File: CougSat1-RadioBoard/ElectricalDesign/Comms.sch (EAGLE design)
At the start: 411 parts, among them J1 230mm Antenna, J2 CougSat Card, J3 700mm Antenna, J4 SWD, Q1 CSD25402Q3A, Q12 DMN53D0LDW, Q2 CSD25402Q3A, Q3 DMN53D0LDW, Q9 DMN53D0LDW, U1 INA199C1, U10 HMC452QS16G, U11 AD8515, U12 AD7291, U13 AD8515, U14 LP5907MFX-3.1, U15 AD9761, U16 TXS0102DQM, U18 TXS0102DQM, U19 MMZ09332B, U2 LP5907MFX-3.1, U20 ADF4360, U21 HMC545A, U22 AD9761, U23 MAAM-011229, U24 AD8515, U25 MAAM-011229, U26 AD8345, U28 AD8348, U29 AD7291, U3 TPS61236, U30 TXS0102DQM, U31 MAAM-011229, U32 AD8515, U35 TXS0102DQM, U36 ADF4360, U37 MAAM-011229, U39 AD8515, U4 AD8346, U40 AD8515, U42 TXS0102DQM, U43 INA199C2, U44 TXS0102DQM, U45 TXS0102DQM, U46 TXS0102DQM, U47 TXS0102DQM, U48 AD7291, U49 AD8515, U5 ADF4360, U50 INA199C2, U51 LP5907MFX-3.1, U52 INA199C2, U53 INA199C1, U54 TXS0102DQM, U55 TXS0102DQM, U6 STM32L496VGT, U7 GRF2133, U8 IS25LP016D, U9 IS25LP016D, Y1 19.68MHz ±2.5ppm, Y2 8MHz ±10ppm, Y3 32.768kHz ±10ppm, Y4 19.68MHz ±2.5ppm, Y5 19.68MHz ±2.5ppm

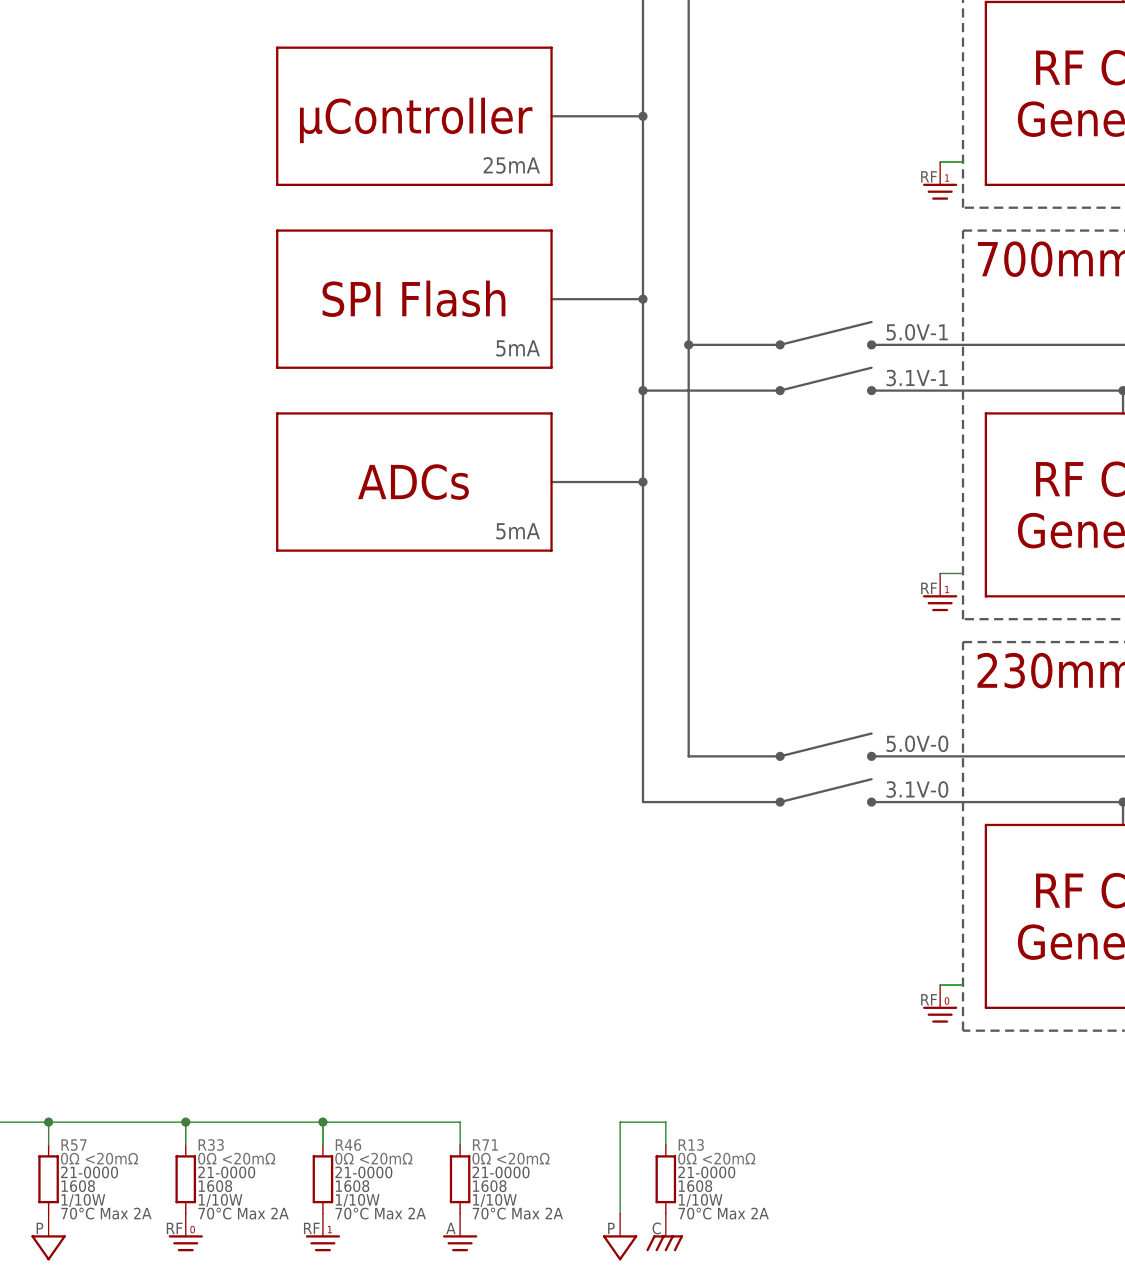
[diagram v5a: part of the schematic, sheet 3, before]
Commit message: Changed isolated ground to a solid DGND and relaying on layout to ensure good layout
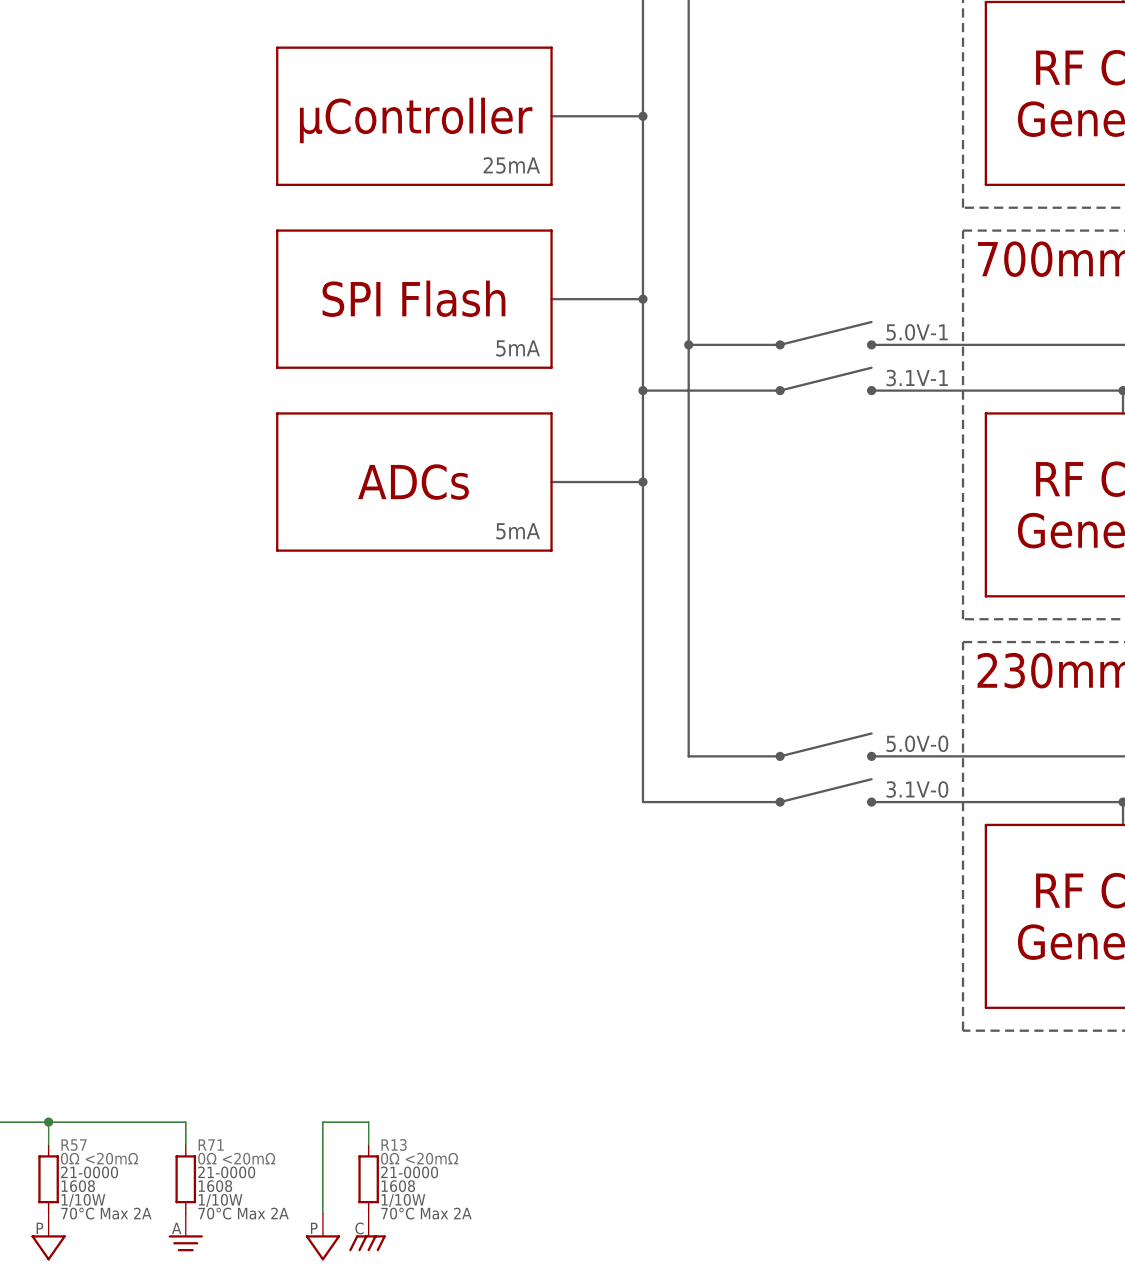
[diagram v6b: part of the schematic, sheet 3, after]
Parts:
- removed R33, R46: 0Ω <20mΩ, CougsInSpace-Resistors:RES-V-0-1608
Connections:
- removed net RFGND-0: C109.2, C114.2, C116.2, C132.2, C151.2, C16.2, C163.2, C18.2, C27.2, C33.2, C34.2, C39.2, C43.2, C51.2, C52.2, C53.2, C54.2, C79.2, C83.2, H4.SHIELD, J1.SHIELD, L13.1, L14.1, L18.1, L21.1, L4.1, R12.1, R19.1, R26.1, R33.1, R50.1, R51.1, R52.1, R55.1, U10.RFGND, U22.AVSS, U22.REFLO, U4.DGND, U4.RFGND, U5.AGND, U5.CPGND, U5.DGND, U5.PAD, U7.RFGND, Y1.GND
- new net N$7: L12.1, R83.1
- net DGND: now also C101.2, C105.2, C108.2, C109.2, C110.2, C111.2, C112.2, C113.2, C114.2, C116.2, C117.2, C118.2, C119.2, C120.2, C121.2, C122.2, C123.2, C124.1, C128.2, C129.2, C130.2, C132.2, C135.2, C136.2, C137.2, C139.2, C140.2, C143.2, C144.2, C145.2, C146.2, C147.2, C148.2, C151.2, C152.2, C153.2, C154.2, C155.2, C156.2, C16.2, C163.2, C18.2, C185.2, C188.2, C189.2, C191.2, C192.2, C194.2, C195.2, C196.2, C198.2, C199.2, C201.2, C204.2, C27.2, C29.2, C3.2, C33.2, C34.2, C35.2, C39.2, C43.2, C44.2, C46.2, C51.2, C52.2, C53.2, C54.2, C55.2, C56.2, C66.2, C67.2, C68.2, C71.2, C72.2, C73.2, C74.2, C79.2, C80.2, C83.2, C85.2, C88.2, C89.2, C90.2, C91.2, C94.2, C96.2, H4.SHIELD, H7.SHIELD, H8.SHIELD, J1.SHIELD, J3.SHIELD, L10.1, L11.1, L13.1, L14.1, L16.1, L18.1, L19.1, L21.1, L4.1, L9.1, Q12A.S, Q12B.S, Q3A.S, Q3B.D, Q3B.G, Q3B.S, Q9A.S, Q9B.S, R112.1, R12.1, R19.1, R2.1, R26.1, R32.1, R38.1, R40.1, R42.1, R45.1, R48.1, R50.1, R51.1, R52.1, R55.1, R61.1, R64.1, R68.1, R69.1, R70.1, R72.1, R77.1, R79.1, R84.1, R85.1, U10.RFGND, U15.AVSS, U15.REFLO, U20.AGND, U20.CPGND, U20.DGND, U20.PAD, U21.RFGND, U22.AVSS, U22.REFLO, U23.RFGND, U25.RFGND, U26.DGND, U26.RFGND, U28.DGND, U28.RFGND, U31.RFGND, U36.AGND, U36.CPGND, U36.DGND, U36.PAD, U37.RFGND, U4.DGND, U4.RFGND, U5.AGND, U5.CPGND, U5.DGND, U5.PAD, U7.RFGND, Y1.GND, Y4.GND, Y5.GND; no longer R33.2, R46.2
- net PGND: no longer C130.2, C3.2, C55.2, C56.2, Q9A.S, Q9B.S, R112.1, R2.1, R32.1, R40.1
- net RFGND-1: no longer C101.2, C105.2, C108.2, C110.2, C111.2, C112.2, C113.2, C117.2, C118.2, C119.2, C120.2, C121.2, C122.2, C123.2, C124.1, C128.2, C129.2, C135.2, C136.2, C137.2, C139.2, C140.2, C143.2, C144.2, C145.2, C146.2, C147.2, C148.2, C152.2, C153.2, C154.2, C155.2, C156.2, C185.2, C188.2, C189.2, C191.2, C192.2, C194.2, C195.2, C196.2, C198.2, C199.2, C201.2, C204.2, C29.2, C35.2, C44.2, C46.2, C66.2, C67.2, C68.2, C71.2, C72.2, C73.2, C74.2, C80.2, C85.2, C88.2, C89.2, C90.2, C91.2, C94.2, C96.2, H7.SHIELD, H8.SHIELD, J3.SHIELD, L10.1, L11.1, L12.1, L16.1, L19.1, L9.1, Q12A.S, Q12B.S, Q3A.S, Q3B.D, Q3B.G, Q3B.S, R38.1, R42.1, R45.1, R46.1, R48.1, R61.1, R64.1, R68.1, R69.1, R70.1, R72.1, R77.1, R79.1, R83.1, R84.1, R85.1, U15.AVSS, U15.REFLO, U20.AGND, U20.CPGND, U20.DGND, U20.PAD, U21.RFGND, U23.RFGND, U25.RFGND, U26.DGND, U26.RFGND, U28.DGND, U28.RFGND, U31.RFGND, U36.AGND, U36.CPGND, U36.DGND, U36.PAD, U37.RFGND, Y4.GND, Y5.GND
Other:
- moved on the sheet: R13, R71

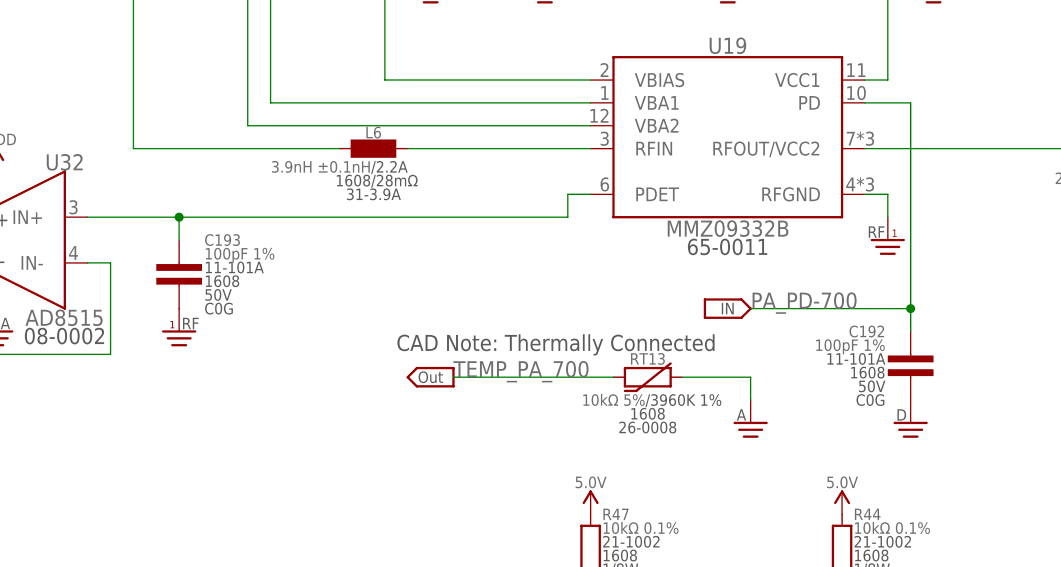
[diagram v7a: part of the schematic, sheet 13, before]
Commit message: Laid out 700mm modulator
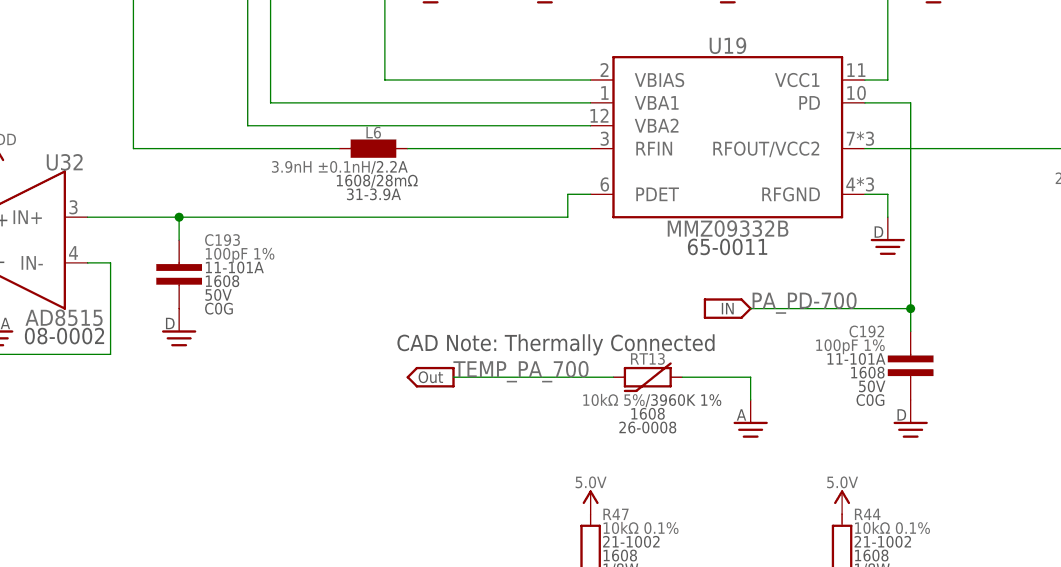
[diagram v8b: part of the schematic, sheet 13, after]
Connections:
- removed net N$7: L12.1, R83.1
- removed net RFGND-1: C193.2, U19.RFGND
- net DGND: now also C193.2, L12.1, R83.1, U19.RFGND
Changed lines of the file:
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@@
 <part name="L20" library="CougsInSpace-Coils" deviceset="INDUCTOR-H" device="-1608" technology="-56NH" value="56nH 2%"/>
 <part name="C67" library="CougsInSpace-Capacitors" deviceset="CAP-V" device="-1608" technology="-47PF" value="47pF 5%"/>
-<part name="SUPPLY246" library="CougsInSpace-PowerSymbols" deviceset="RFGND-1" device=""/>
-<part name="SUPPLY247" library="CougsInSpace-PowerSymbols" deviceset="RFGND-1" device=""/>
 <part name="C202" library="CougsInSpace-Capacitors" deviceset="CAP-H" device="-1608" technology="-220PF" value="220pF 1%"/>
 <part name="SUPPLY263" library="CougsInSpace-PowerSymbols" deviceset="5.0V-1" device=""/>
@@
 <part name="SUPPLY309" library="CougsInSpace-PowerSymbols" deviceset="DGND" device=""/>
 <part name="SUPPLY310" library="CougsInSpace-PowerSymbols" deviceset="DGND" device=""/>
+<part name="SUPPLY246" library="CougsInSpace-PowerSymbols" deviceset="DGND" device=""/>
+<part name="SUPPLY247" library="CougsInSpace-PowerSymbols" deviceset="DGND" device=""/>
+<part name="SUPPLY325" library="CougsInSpace-PowerSymbols" deviceset="DGND" device=""/>
 </parts>
 <sheets>
@@
 <instance part="SUPPLY191" gate="1" x="83.82" y="162.56" smashed="yes"/>
 <instance part="SUPPLY198" gate="1" x="20.32" y="170.18" smashed="yes"/>
+<instance part="SUPPLY325" gate="1" x="218.44" y="132.08" smashed="yes"/>
 </instances>
 <busses>
@@
 <pinref part="SUPPLY198" gate="1" pin="DGND"/>
 </segment>
+<segment>
+<pinref part="L12" gate="G$1" pin="1"/>
+<wire x1="218.44" y1="134.62" x2="218.44" y2="137.16" width="0.1524" layer="91"/>
+<pinref part="R83" gate="G$1" pin="1"/>
+<wire x1="218.44" y1="137.16" x2="218.44" y2="139.7" width="0.1524" layer="91"/>
+<wire x1="218.44" y1="137.16" x2="228.6" y2="137.16" width="0.1524" layer="91"/>
+<wire x1="228.6" y1="137.16" x2="228.6" y2="139.7" width="0.1524" layer="91"/>
+<junction x="218.44" y="137.16"/>
+<pinref part="SUPPLY325" gate="1" pin="DGND"/>
+</segment>
 </net>
 <net name="MOD_SCK" class="0">
@@
 </segment>
 </net>
-<net name="N$7" class="0">
-<segment>
-<pinref part="L12" gate="G$1" pin="1"/>
-<wire x1="218.44" y1="134.62" x2="218.44" y2="137.16" width="0.1524" layer="91"/>
-<pinref part="R83" gate="G$1" pin="1"/>
-<wire x1="218.44" y1="137.16" x2="218.44" y2="139.7" width="0.1524" layer="91"/>
-<wire x1="218.44" y1="137.16" x2="228.6" y2="137.16" width="0.1524" layer="91"/>
-<wire x1="228.6" y1="137.16" x2="228.6" y2="139.7" width="0.1524" layer="91"/>
-<junction x="218.44" y="137.16"/>
-</segment>
-</net>
 </nets>
 </sheet>
@@
 <attribute name="TEMP" x="249.174" y="170.18" size="1.27" layer="97" align="center-left"/>
 </instance>
-<instance part="SUPPLY246" gate="G$1" x="63.5" y="60.96" smashed="yes" rot="MR0"/>
-<instance part="SUPPLY247" gate="G$1" x="142.24" y="71.12" smashed="yes"/>
 <instance part="C202" gate="G$1" x="170.18" y="81.28" smashed="yes">
 <attribute name="NAME" x="168.91" y="84.582" size="1.27" layer="95" align="center"/>
@@
 <instance part="SUPPLY259" gate="1" x="15.24" y="7.62" smashed="yes"/>
 <instance part="SUPPLY260" gate="1" x="30.48" y="7.62" smashed="yes"/>
+<instance part="SUPPLY246" gate="1" x="63.5" y="60.96" smashed="yes"/>
+<instance part="SUPPLY247" gate="1" x="142.24" y="71.12" smashed="yes"/>
 </instances>
 <busses>
@@
 </segment>
 </net>
-<net name="RFGND-1" class="3">
-<segment>
-<pinref part="C193" gate="G$1" pin="2"/>
-<pinref part="SUPPLY246" gate="G$1" pin="RFGND-1"/>
-</segment>
-<segment>
-<pinref part="U19" gate="G$1" pin="RFGND"/>
-<pinref part="SUPPLY247" gate="G$1" pin="RFGND-1"/>
-<wire x1="139.7" y1="76.2" x2="142.24" y2="76.2" width="0.1524" layer="91"/>
-<wire x1="142.24" y1="76.2" x2="142.24" y2="73.66" width="0.1524" layer="91"/>
-</segment>
-</net>
 <net name="5.0V" class="3">
 <segment>
@@
 <pinref part="SUPPLY260" gate="1" pin="DGND"/>
 </segment>
+<segment>
+<pinref part="C193" gate="G$1" pin="2"/>
+<pinref part="SUPPLY246" gate="1" pin="DGND"/>
+</segment>
+<segment>
+<pinref part="U19" gate="G$1" pin="RFGND"/>
+<wire x1="139.7" y1="76.2" x2="142.24" y2="76.2" width="0.1524" layer="91"/>
+<wire x1="142.24" y1="76.2" x2="142.24" y2="73.66" width="0.1524" layer="91"/>
+<pinref part="SUPPLY247" gate="1" pin="DGND"/>
+</segment>
 </net>
